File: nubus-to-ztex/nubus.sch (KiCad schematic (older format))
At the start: 54 parts, among them J4 C96ABC, U1 74LVT125, U13 SN74CB3T3245PWR, U14 SN74CB3T3245PWR, U15 SN74CB3T3245PWR, U2 74LVT125, U3 74LVT125, U5 74LVT245BPW,118, U6 74LVT245BPW,118, U7 74LVT245BPW,118, U8 74LVT245BPW,118

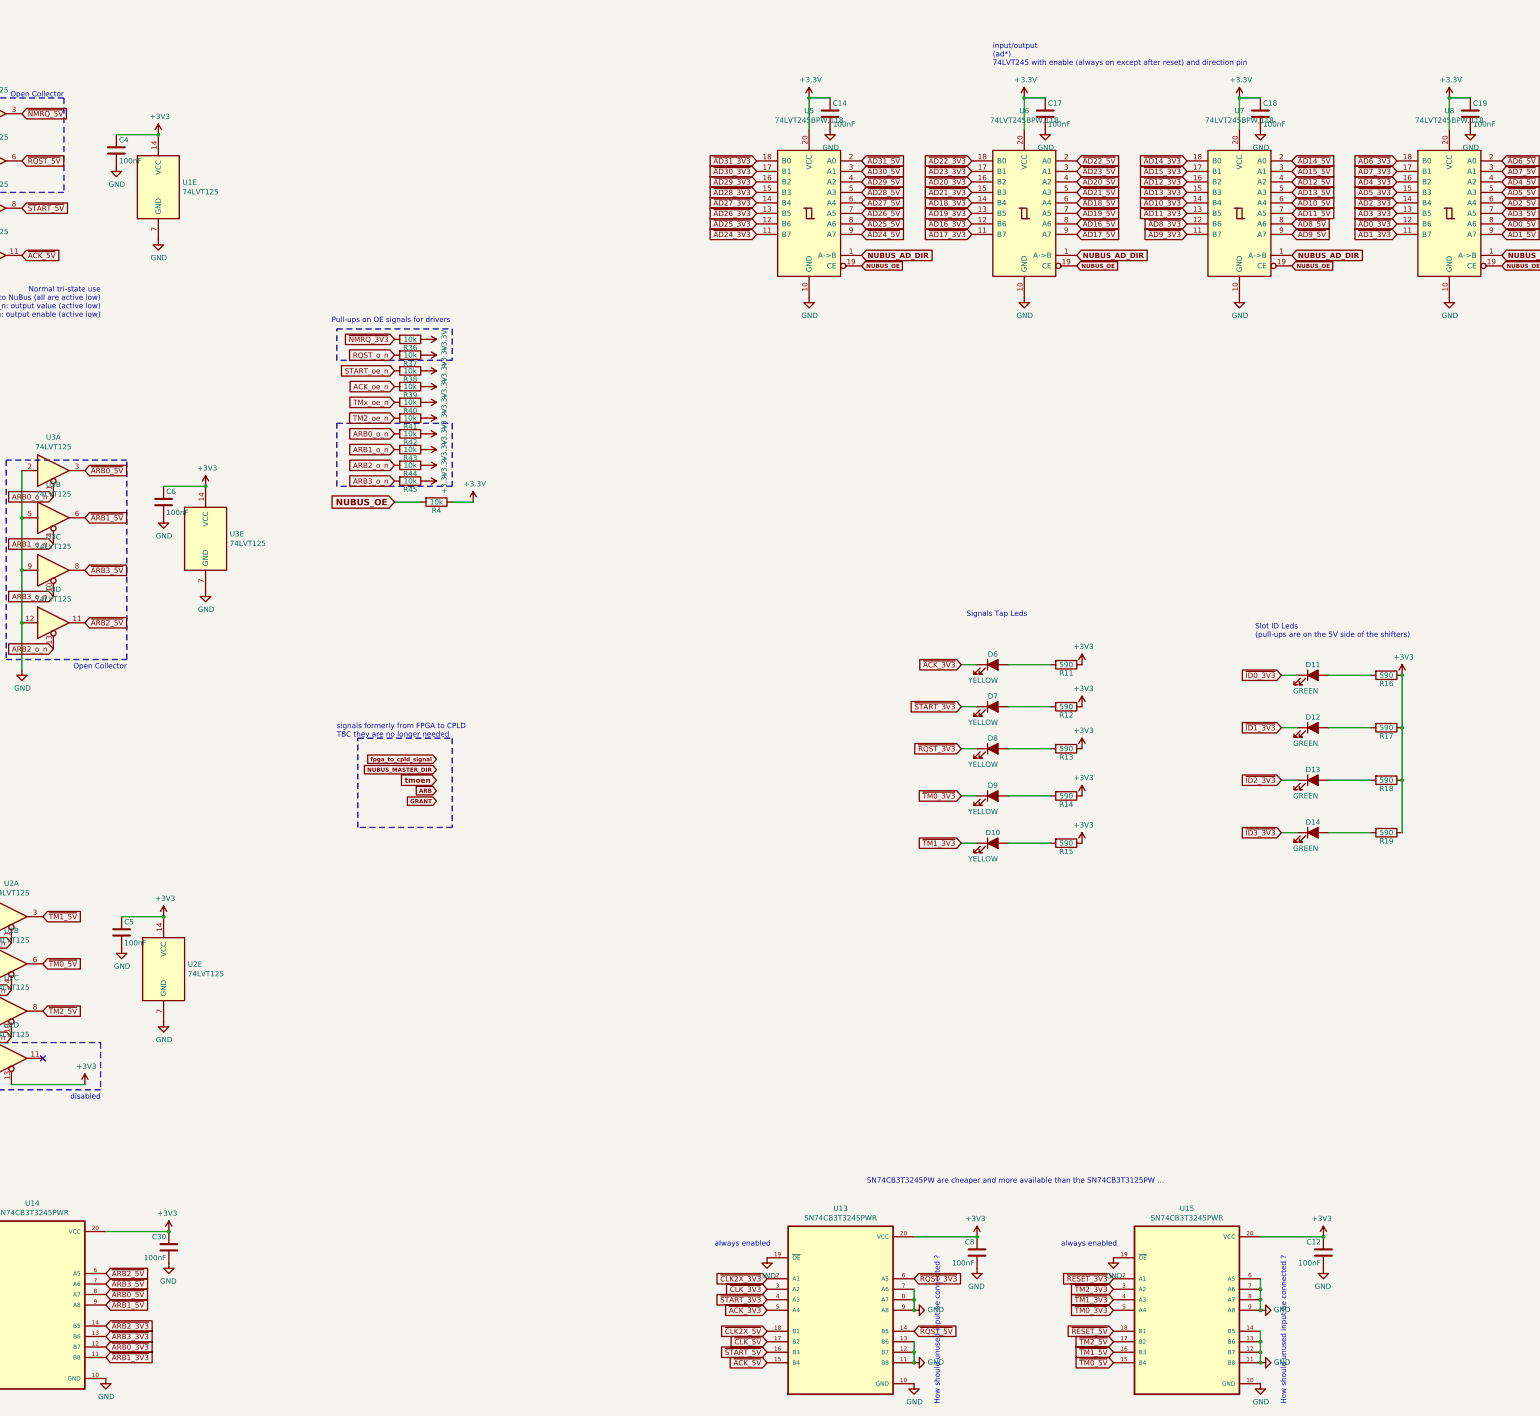
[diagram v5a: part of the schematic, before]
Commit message: move shielding to hdmi, trace cleanup
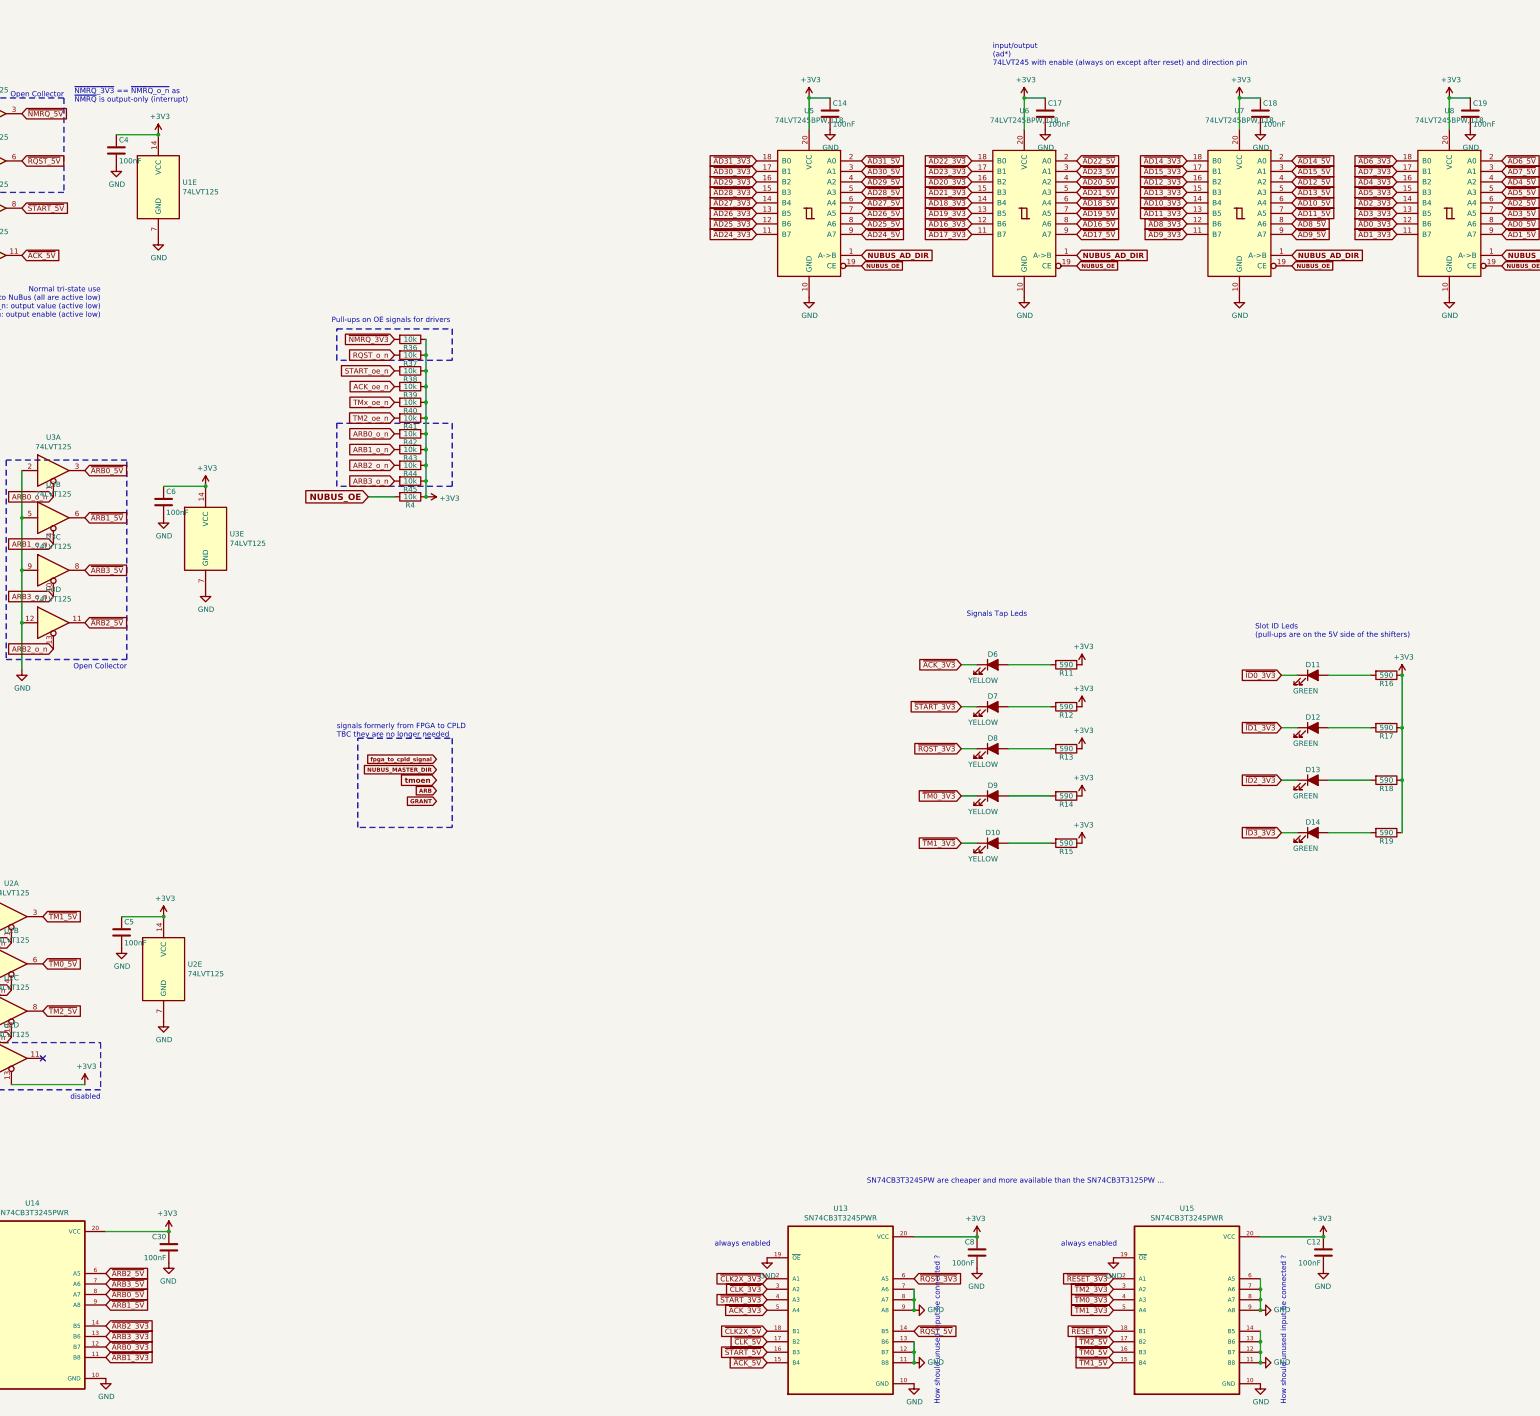
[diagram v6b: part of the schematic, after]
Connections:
- net ~TM0_3V3: now also U15.4 (A3); no longer U15.5 (A4)
- net ~TM0_5V: now also U15.16 (B3); no longer U15.15 (B4)
- net ~TM1_3V3: now also U15.5 (A4); no longer U15.4 (A3)
- net ~TM1_5V: now also U15.15 (B4); no longer U15.16 (B3)
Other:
- note added: "~NMRQ_3V3~ == ~NMRQ_o_n~ as\n~NMRQ~ is output-only (interrupt)"
- moved on the sheet: R4
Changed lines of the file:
@@
 $Descr A2 23386 16535
 encoding utf-8
-Sheet 3 9
+Sheet 3 8
 Title "nubus-to-ztex NuBus connection & level shifting"
 Date ""
@@
 $EndComp
 $Comp
-L power:+3.3V #PWR056
-U 1 1 5F8CA5D4
-P 17350 2350
-F 0 "#PWR056" H 17350 2200 50  0001 C CNN
-F 1 "+3.3V" H 17365 2523 50  0000 C CNN
-F 2 "" H 17350 2350 50  0001 C CNN
-F 3 "" H 17350 2350 50  0001 C CNN
-	1    17350 2350
-	1    0    0    -1
-$EndComp
-$Comp
 L power:GND #PWR057
 U 1 1 5F8CA5DA
@@
 	1    0    0    -1
 $EndComp
-$Comp
-L power:+3.3V #PWR025
-U 1 1 5F91B88F
-P 8050 6200
-F 0 "#PWR025" H 8050 6050 50  0001 C CNN
-F 1 "+3.3V" H 8065 6373 50  0000 C CNN
-F 2 "" H 8050 6200 50  0001 C CNN
-F 3 "" H 8050 6200 50  0001 C CNN
-	1    8050 6200
-	1    0    0    -1
-$EndComp
-Text GLabel 7300 6200 0    60   Input ~ 12
+Text GLabel 7050 6150 0    60   Input ~ 12
 NUBUS_OE
 $Comp
 L Device:R R?
 U 1 1 5F93CF72
-P 7700 6200
+P 7450 6150
 AR Path="/5F6B165A/5F93CF72" Ref="R?"  Part="1"
 AR Path="/5F679B53/5F93CF72" Ref="R?"  Part="1"
 AR Path="/618F532C/5F93CF72" Ref="R4"  Part="1"
-F 0 "R4" V 7780 6200 50  0000 C CNN
-F 1 "10k" V 7700 6200 50  0000 C CNN
-F 2 "Resistor_SMD:R_0603_1608Metric" V 7630 6200 50  0001 C CNN
-F 3 "" H 7700 6200 50  0000 C CNN
-F 4 "0603WAF1002T5E" V 7700 5600 50  0001 C CNN "MPN"
-	1    7700 6200
-	0    1    1    0
-$EndComp
-Wire Wire Line
-	7550 6200 7300 6200
+F 0 "R4" V 7530 6150 50  0000 C CNN
+F 1 "10k" V 7450 6150 50  0000 C CNN
+F 2 "Resistor_SMD:R_0603_1608Metric" V 7380 6150 50  0001 C CNN
+F 3 "" H 7450 6150 50  0000 C CNN
+F 4 "0603WAF1002T5E" V 7450 5550 50  0001 C CNN "MPN"
+	1    7450 6150
+	0    1    1    0
+$EndComp
+Wire Wire Line
+	7300 6150 7050 6150
 $Comp
 L C96ABC:C96ABC_NUBUS J4
@@
 Connection ~ 2350 14250
 Wire Wire Line
-	7850 6200 8050 6200
-Wire Wire Line
 	2250 14250 2050 14250
 Connection ~ 2250 14250
@@
 Wire Wire Line
 	17350 2650 17350 2350
-Connection ~ 17350 2350
 $Comp
 L Device:C C18
@@
 $EndComp
 $Comp
-L power:+3.3V #PWR047
-U 1 1 61BCFF4D
-P 15350 2350
-F 0 "#PWR047" H 15350 2200 50  0001 C CNN
-F 1 "+3.3V" H 15365 2523 50  0000 C CNN
-F 2 "" H 15350 2350 50  0001 C CNN
-F 3 "" H 15350 2350 50  0001 C CNN
-	1    15350 2350
-	1    0    0    -1
-$EndComp
-$Comp
 L power:GND #PWR048
 U 1 1 61BCFF53
@@
 Wire Wire Line
 	15350 2650 15350 2350
-Connection ~ 15350 2350
 $Comp
 L Device:C C17
@@
 $EndComp
 $Comp
-L power:+3.3V #PWR042
-U 1 1 61BD1F01
-P 13300 2350
-F 0 "#PWR042" H 13300 2200 50  0001 C CNN
-F 1 "+3.3V" H 13315 2523 50  0000 C CNN
-F 2 "" H 13300 2350 50  0001 C CNN
-F 3 "" H 13300 2350 50  0001 C CNN
-	1    13300 2350
-	1    0    0    -1
-$EndComp
-$Comp
 L power:GND #PWR043
 U 1 1 61BD1F07
@@
 Wire Wire Line
 	13300 2650 13300 2350
-Connection ~ 13300 2350
 $Comp
 L Device:C C14
@@
 F 3 "" H 11450 2650 50  0001 C CNN
 	1    11450 2650
-	1    0    0    -1
-$EndComp
-$Comp
-L power:+3.3V #PWR039
-U 1 1 61BD1F2E
-P 11250 2350
-F 0 "#PWR039" H 11250 2200 50  0001 C CNN
-F 1 "+3.3V" H 11265 2523 50  0000 C CNN
-F 2 "" H 11250 2350 50  0001 C CNN
-F 3 "" H 11250 2350 50  0001 C CNN
-	1    11250 2350
 	1    0    0    -1
 $EndComp
@@
 Wire Wire Line
 	11250 2650 11250 2350
-Connection ~ 11250 2350
 Text GLabel 17850 3850 2    50   Input ~ 10
 NUBUS_AD_DIR
@@
 Text Notes 13000 2050 0    50   ~ 0
 input/output\n(ad*)\n74LVT245 with enable (always on except after reset) and direction pin
+Text GLabel 14150 14400 0    50   Input ~ 0
+~TM1_5V
 Text GLabel 14150 14300 0    50   Input ~ 0
-~TM1_5V
-Text GLabel 14150 14400 0    50   Input ~ 0
 ~TM0_5V
+Text GLabel 14150 13900 0    50   Input ~ 0
+~TM1_3V3
 Text GLabel 14150 13800 0    50   Input ~ 0
-~TM1_3V3
-Text GLabel 14150 13900 0    50   Input ~ 0
 ~TM0_3V3
 Wire Wire Line
@@
 ARB2_o_n
 $Comp
-L power:+3.3V #PWR0132
-U 1 1 621BDDC4
-P 7600 4650
-F 0 "#PWR0132" H 7600 4500 50  0001 C CNN
-F 1 "+3.3V" H 7615 4823 50  0000 C CNN
-F 2 "" H 7600 4650 50  0001 C CNN
-F 3 "" H 7600 4650 50  0001 C CNN
-	1    7600 4650
-	0    1    1    0
-$EndComp
-$Comp
 L Device:R R?
 U 1 1 621BDDCB
@@
 $EndComp
 $Comp
-L power:+3.3V #PWR0133
-U 1 1 621C4810
-P 7600 4800
-F 0 "#PWR0133" H 7600 4650 50  0001 C CNN
-F 1 "+3.3V" H 7615 4973 50  0000 C CNN
-F 2 "" H 7600 4800 50  0001 C CNN
-F 3 "" H 7600 4800 50  0001 C CNN
-	1    7600 4800
-	0    1    1    0
-$EndComp
-$Comp
 L Device:R R?
 U 1 1 621C4817
@@
 $EndComp
 $Comp
-L power:+3.3V #PWR0134
-U 1 1 621C7B0F
-P 7600 4950
-F 0 "#PWR0134" H 7600 4800 50  0001 C CNN
-F 1 "+3.3V" H 7615 5123 50  0000 C CNN
-F 2 "" H 7600 4950 50  0001 C CNN
-F 3 "" H 7600 4950 50  0001 C CNN
-	1    7600 4950
-	0    1    1    0
-$EndComp
-$Comp
 L Device:R R?
 U 1 1 621C7B16
@@
 $EndComp
 $Comp
-L power:+3.3V #PWR0135
-U 1 1 621CAE0C
-P 7600 5100
-F 0 "#PWR0135" H 7600 4950 50  0001 C CNN
-F 1 "+3.3V" H 7615 5273 50  0000 C CNN
-F 2 "" H 7600 5100 50  0001 C CNN
-F 3 "" H 7600 5100 50  0001 C CNN
-	1    7600 5100
-	0    1    1    0
-$EndComp
-$Comp
 L Device:R R?
 U 1 1 621CAE13
@@
 $EndComp
 $Comp
-L power:+3.3V #PWR0136
-U 1 1 621CE107
-P 7600 5250
-F 0 "#PWR0136" H 7600 5100 50  0001 C CNN
-F 1 "+3.3V" H 7615 5423 50  0000 C CNN
-F 2 "" H 7600 5250 50  0001 C CNN
-F 3 "" H 7600 5250 50  0001 C CNN
-	1    7600 5250
-	0    1    1    0
-$EndComp
-$Comp
 L Device:R R?
 U 1 1 621CE10E
@@
 $EndComp
 $Comp
-L power:+3.3V #PWR0137
-U 1 1 621D1400
-P 7600 5400
-F 0 "#PWR0137" H 7600 5250 50  0001 C CNN
-F 1 "+3.3V" H 7615 5573 50  0000 C CNN
-F 2 "" H 7600 5400 50  0001 C CNN
-F 3 "" H 7600 5400 50  0001 C CNN
-	1    7600 5400
-	0    1    1    0
-$EndComp
-$Comp
 L Device:R R?
 U 1 1 621D1407
@@
 $EndComp
 $Comp
-L power:+3.3V #PWR0138
-U 1 1 621D46FD
-P 7600 5550
-F 0 "#PWR0138" H 7600 5400 50  0001 C CNN
-F 1 "+3.3V" H 7615 5723 50  0000 C CNN
-F 2 "" H 7600 5550 50  0001 C CNN
-F 3 "" H 7600 5550 50  0001 C CNN
-	1    7600 5550
-	0    1    1    0
-$EndComp
-$Comp
 L Device:R R?
 U 1 1 621D4704
@@
 $EndComp
 $Comp
-L power:+3.3V #PWR0139
-U 1 1 621D79FA
-P 7600 5700
-F 0 "#PWR0139" H 7600 5550 50  0001 C CNN
-F 1 "+3.3V" H 7615 5873 50  0000 C CNN
-F 2 "" H 7600 5700 50  0001 C CNN
-F 3 "" H 7600 5700 50  0001 C CNN
-	1    7600 5700
-	0    1    1    0
-$EndComp
-$Comp
 L Device:R R?
 U 1 1 621D7A01
@@
 $EndComp
 $Comp
-L power:+3.3V #PWR0140
-U 1 1 621DACF9
-P 7600 5850
-F 0 "#PWR0140" H 7600 5700 50  0001 C CNN
-F 1 "+3.3V" H 7615 6023 50  0000 C CNN
-F 2 "" H 7600 5850 50  0001 C CNN
-F 3 "" H 7600 5850 50  0001 C CNN
-	1    7600 5850
-	0    1    1    0
-$EndComp
-$Comp
 L Device:R R?
 U 1 1 621DAD00
@@
 F 4 "0603WAF1002T5E" V 7450 5250 50  0001 C CNN "MPN"
 	1    7450 5850
-	0    1    1    0
-$EndComp
-$Comp
-L power:+3.3V #PWR0141
-U 1 1 621DDFF8
-P 7600 6000
-F 0 "#PWR0141" H 7600 5850 50  0001 C CNN
-F 1 "+3.3V" H 7615 6173 50  0000 C CNN
-F 2 "" H 7600 6000 50  0001 C CNN
-F 3 "" H 7600 6000 50  0001 C CNN
-	1    7600 6000
 	0    1    1    0
 $EndComp
@@
 $EndComp
 Connection ~ 15550 14400
+Text Notes 4250 2400 0    50   ~ 0
+~NMRQ_3V3~ == ~NMRQ_o_n~ as\n~NMRQ~ is output-only (interrupt)
+$Comp
+L power:+3V3 #PWR0111
+U 1 1 6343D2A1
+P 17350 2350
+F 0 "#PWR0111" H 17350 2200 50  0001 C CNN
+F 1 "+3V3" H 17365 2523 50  0000 C CNN
+F 2 "" H 17350 2350 50  0001 C CNN
+F 3 "" H 17350 2350 50  0001 C CNN
+	1    17350 2350
+	1    0    0    -1
+$EndComp
+Connection ~ 17350 2350
+$Comp
+L power:+3V3 #PWR0126
+U 1 1 6343E4A3
+P 15350 2350
+F 0 "#PWR0126" H 15350 2200 50  0001 C CNN
+F 1 "+3V3" H 15365 2523 50  0000 C CNN
+F 2 "" H 15350 2350 50  0001 C CNN
+F 3 "" H 15350 2350 50  0001 C CNN
+	1    15350 2350
+	1    0    0    -1
+$EndComp
+Connection ~ 15350 2350
+$Comp
+L power:+3V3 #PWR0127
+U 1 1 6343E927
+P 13300 2350
+F 0 "#PWR0127" H 13300 2200 50  0001 C CNN
+F 1 "+3V3" H 13315 2523 50  0000 C CNN
+F 2 "" H 13300 2350 50  0001 C CNN
+F 3 "" H 13300 2350 50  0001 C CNN
+	1    13300 2350
+	1    0    0    -1
+$EndComp
+Connection ~ 13300 2350
+$Comp
+L power:+3V3 #PWR0128
+U 1 1 6343EC61
+P 11250 2350
+F 0 "#PWR0128" H 11250 2200 50  0001 C CNN
+F 1 "+3V3" H 11265 2523 50  0000 C CNN
+F 2 "" H 11250 2350 50  0001 C CNN
+F 3 "" H 11250 2350 50  0001 C CNN
+	1    11250 2350
+	1    0    0    -1
+$EndComp
+Connection ~ 11250 2350
+Wire Wire Line
+	7600 6000 7600 5850
+Wire Wire Line
+	7600 5850 7600 5700
+Connection ~ 7600 5850
+Wire Wire Line
+	7600 5700 7600 5550
+Connection ~ 7600 5700
+Wire Wire Line
+	7600 5550 7600 5400
+Connection ~ 7600 5550
+Wire Wire Line
+	7600 5250 7600 5100
+Wire Wire Line
+	7600 5400 7600 5250
+Connection ~ 7600 5400
+Connection ~ 7600 5250
+Wire Wire Line
+	7600 5100 7600 4950
+Connection ~ 7600 5100
+Wire Wire Line
+	7600 4950 7600 4800
+Connection ~ 7600 4950
+Wire Wire Line
+	7600 4800 7600 4650
+Connection ~ 7600 4800
+Wire Wire Line
+	7600 6150 7600 6000
+Connection ~ 7600 6000
+$Comp
+L power:+3V3 #PWR0131
+U 1 1 6345156A
+P 7600 6150
+F 0 "#PWR0131" H 7600 6000 50  0001 C CNN
+F 1 "+3V3" V 7615 6278 50  0000 L CNN
+F 2 "" H 7600 6150 50  0001 C CNN
+F 3 "" H 7600 6150 50  0001 C CNN
+	1    7600 6150
+	0    1    1    0
+$EndComp
+Connection ~ 7600 6150
 $EndSCHEMATC

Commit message: update everything
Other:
- note added: "SN74CB3T3245PW are cheaper and more available than the (smaller) SN74CB3T3125PW ..."
- note removed: "SN74CB3T3245PW are cheaper and more available than the SN74CB3T3125PW ..."
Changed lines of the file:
@@
 EESchema Schematic File Version 4
-LIBS:nubus-to-ztex-cache
-EELAYER 26 0
+EELAYER 30 0
 EELAYER END
 $Descr A2 23386 16535
@@
 How should unused input be connected ?
 Text Notes 11800 12700 0    50   ~ 0
-SN74CB3T3245PW are cheaper and more available than the SN74CB3T3125PW ...
+SN74CB3T3245PW are cheaper and more available than the (smaller) SN74CB3T3125PW ...
 Connection ~ 12250 13800
 Connection ~ 12250 13900
